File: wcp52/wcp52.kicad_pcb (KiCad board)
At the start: 4 copper layers, 100 x 100 mm, 337 parts, among them J1 MicroUSB-B, J2 IN1, J3 IN2, J4 OUT, J5 9V 300mA, J6 JLINK, J7 AUX, J8 AVR-ICSP, Q1 MMBT3906, Q10 MMBT3904, Q11 BFR540, Q12 BFR540, Q13 MMBT3904, Q14 MMBT3904, Q15 MMBT3904, Q16 MMBT3904, Q17 PZT2907A, Q18 PZT2907A, Q19 MMBT3904, Q2 IRLML6402, Q20 IRLML6402, Q3 AOD417, Q4 MMBT3906, Q5 2N7002, Q6 2N7002, Q7 MMBT3906, Q8 2N7002, Q9 2N7002, U1 TL431AIDBZ, U10 MASWSS0162, U11 AD8310ARMZ, U12 ATSAM4S16CA-AU, U13 FT230XS_DNP, U14 L78M05CDT, U15 MC79M05CDT, U16 AZ1117CH-1.8TRG1, U17 MCP1700T-vv02E/TT, U18 ATMEGA32U4-AU-DNP, U2 LM393M, U3 LMH6714MF, U4 AD9958BCPZ, U5 LMH6714MF, U6 AD8000YRDZ, U7 THS3001IDGN, U8 MAADSS0008, U9 MASWSS0162, X1 25 MHz, X2 12MHz

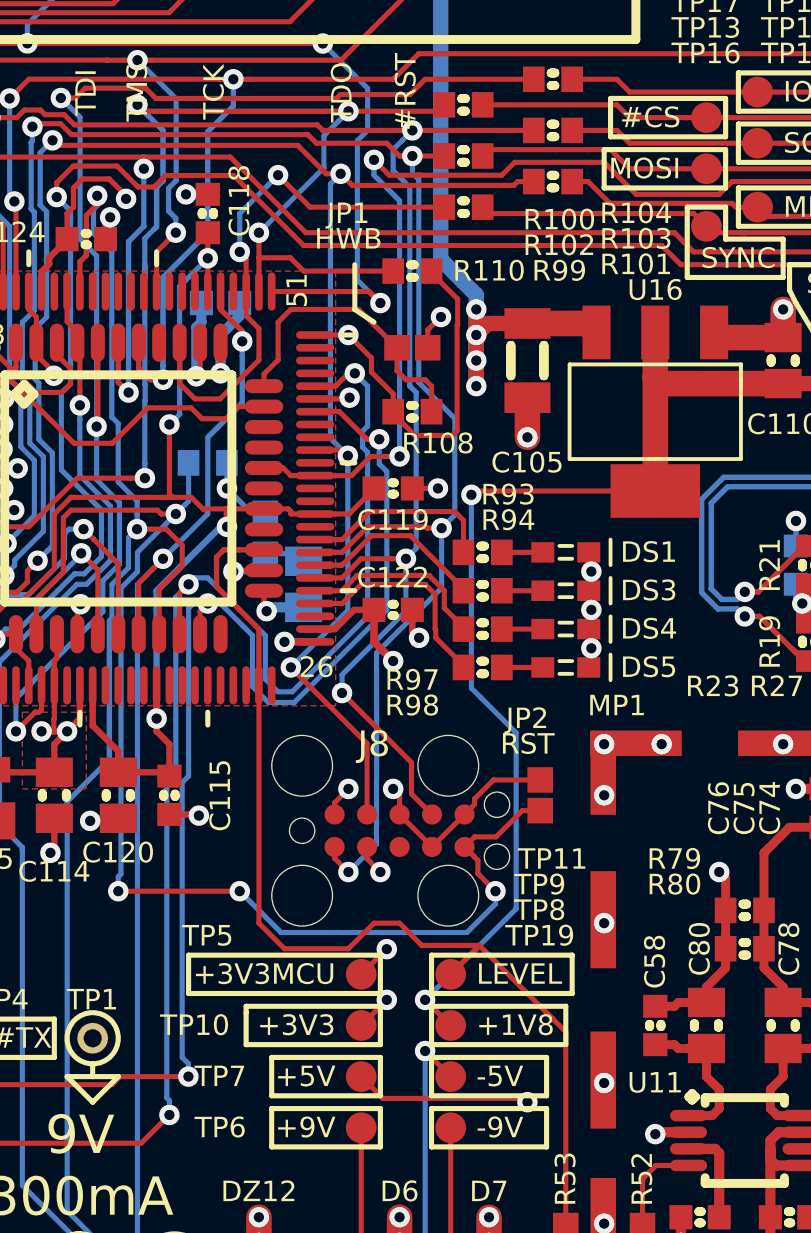
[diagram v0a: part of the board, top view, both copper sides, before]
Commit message: Route LEDs to AVR
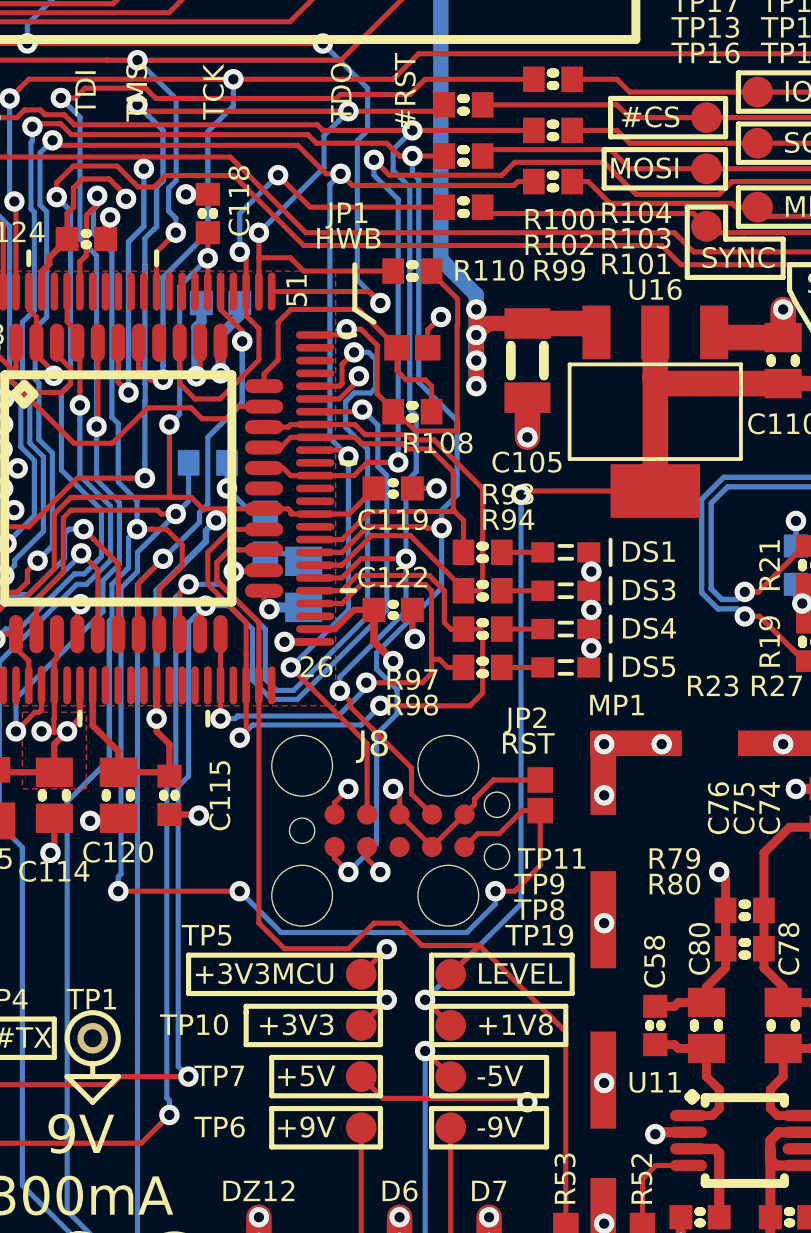
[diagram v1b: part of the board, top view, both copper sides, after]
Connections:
- J6 pad 1: Net-(J6-Pad1) -> +3.3SB
- J6 pad 17: (no net) -> Net-(J6-Pad17)
- U12 pad 21: Net-(U12-Pad21) -> /MPU/LED3
- U12 pad 23: Net-(U12-Pad23) -> /MPU/LED2
- U12 pad 42: Net-(U12-Pad42) -> /MPU/LED0
- U12 pad 43: Net-(U12-Pad43) -> /MPU/LED1
- U18 pad 22: Net-(U18-Pad22) -> /MPU/LED3
- U18 pad 26: Net-(U18-Pad26) -> /MPU/LED2
- U18 pad 30: Net-(U18-Pad30) -> /MPU/LED0
- U18 pad 31: Net-(U18-Pad31) -> /MPU/LED1
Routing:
- net /MPU/LED2: track 7.36 -> 31.6 mm, vias 0 -> 2
- net /MPU/LED1: track 7.21 -> 21.5 mm
- net /MPU/LED3: track 8.48 -> 22.1 mm, vias 0 -> 2
- net /MPU/LED0: track 7.65 -> 17.3 mm
- net /Comm/SER_FROMUSB: track 56.9 -> 59.9 mm
- net +1.8: track 64.4 -> 61.8 mm
- net /MPU/AVR#RST: track 49.6 -> 51.7 mm
- net /MPU/MOSI: track 73.8 -> 74.5 mm
- net GND: track 668.4 -> 669.0 mm

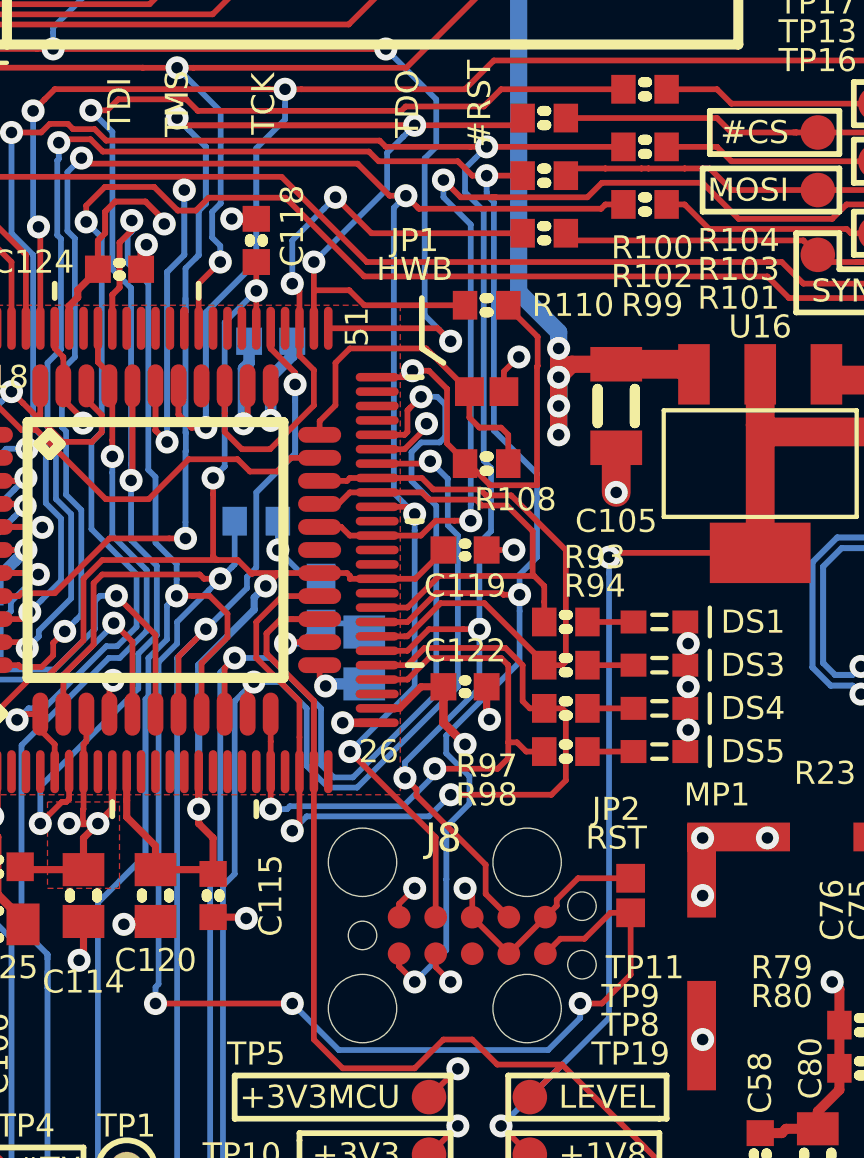
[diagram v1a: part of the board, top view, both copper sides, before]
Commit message: Remove extra connections
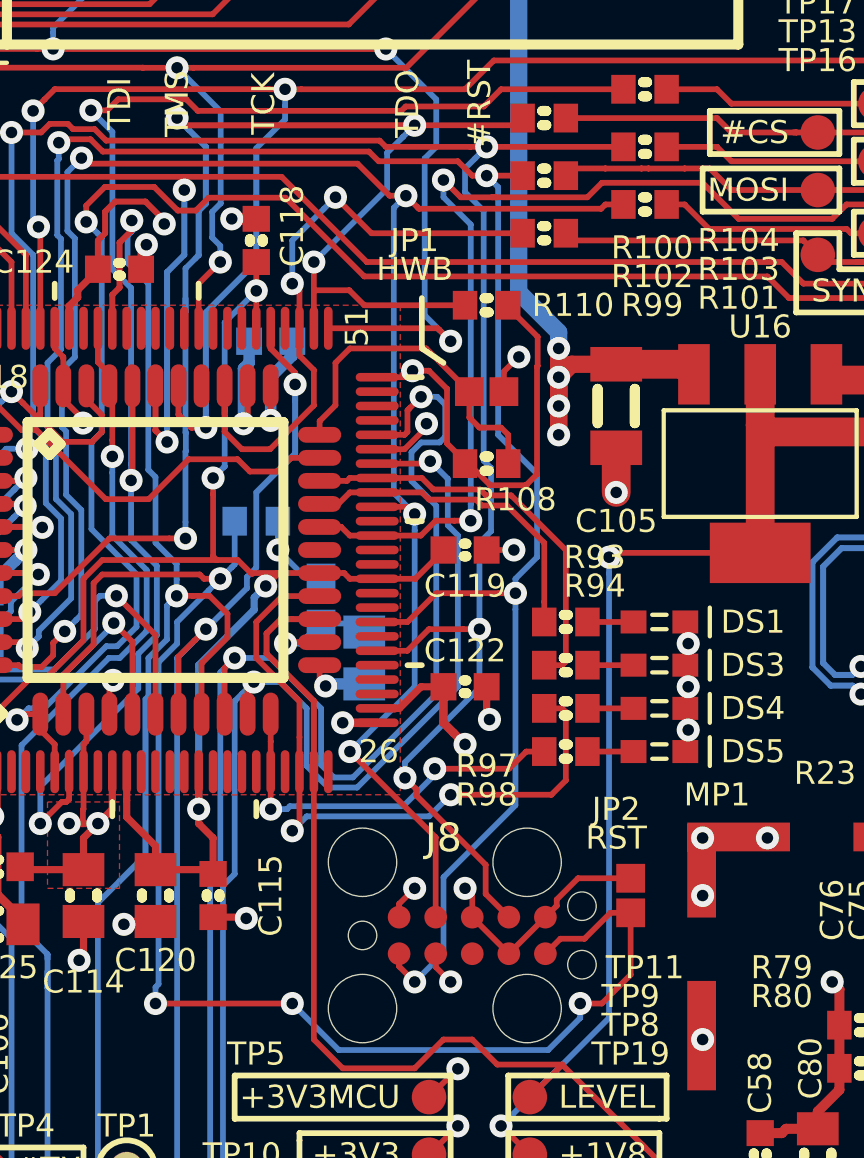
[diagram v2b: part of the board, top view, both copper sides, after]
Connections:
- U12 pad 29: /MPU/LED3 -> Net-(U12-Pad29)
- U12 pad 30: /MPU/LED2 -> Net-(U12-Pad30)
- U12 pad 32: /MPU/LED1 -> Net-(U12-Pad32)
- U12 pad 34: /MPU/LED0 -> Net-(U12-Pad34)
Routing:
- net /MPU/LED3: track 22.1 -> 13.8 mm
- net /MPU/LED2: track 31.6 -> 23.9 mm
- net /MPU/LED1: track 21.5 -> 14.4 mm
- net /MPU/LED0: track 17.3 -> 11.4 mm
- net /MPU/MOSI: track 74.5 -> 73.7 mm

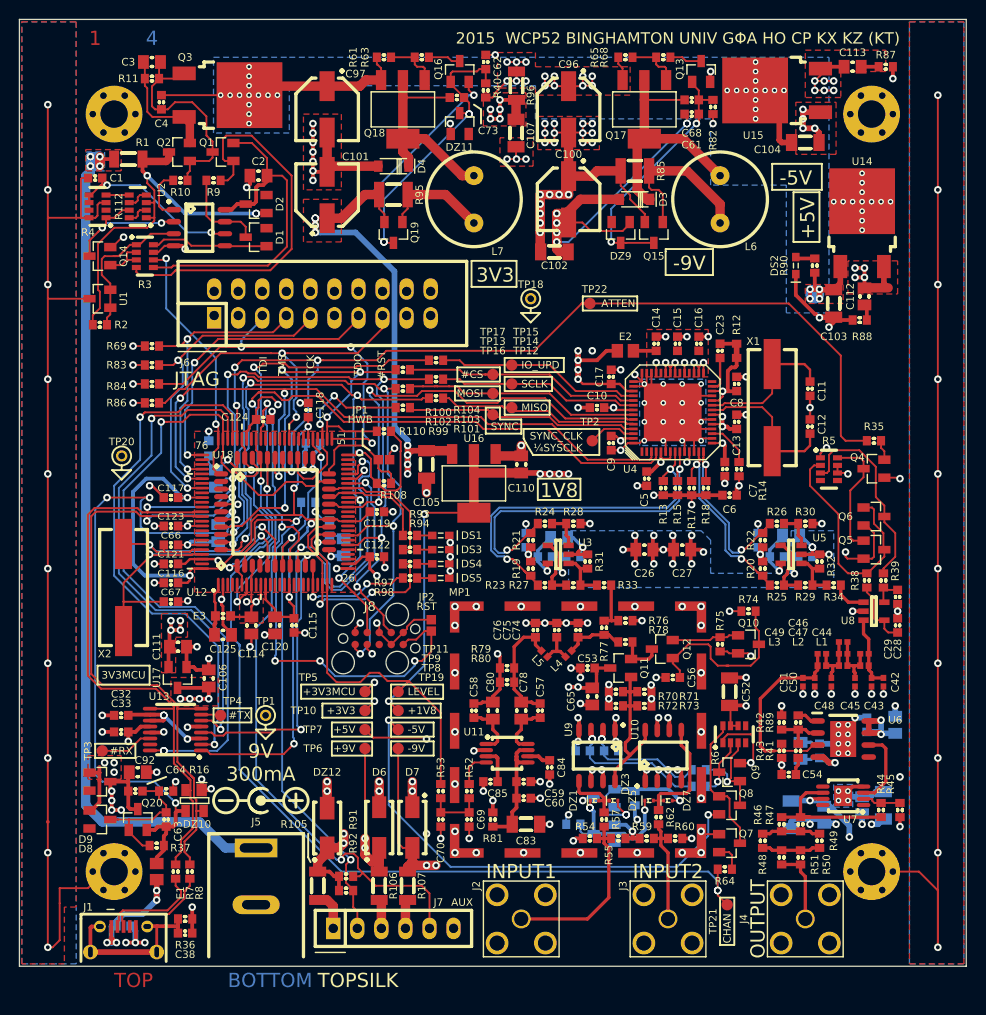
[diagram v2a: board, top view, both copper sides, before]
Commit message: Add PSU filter inductors
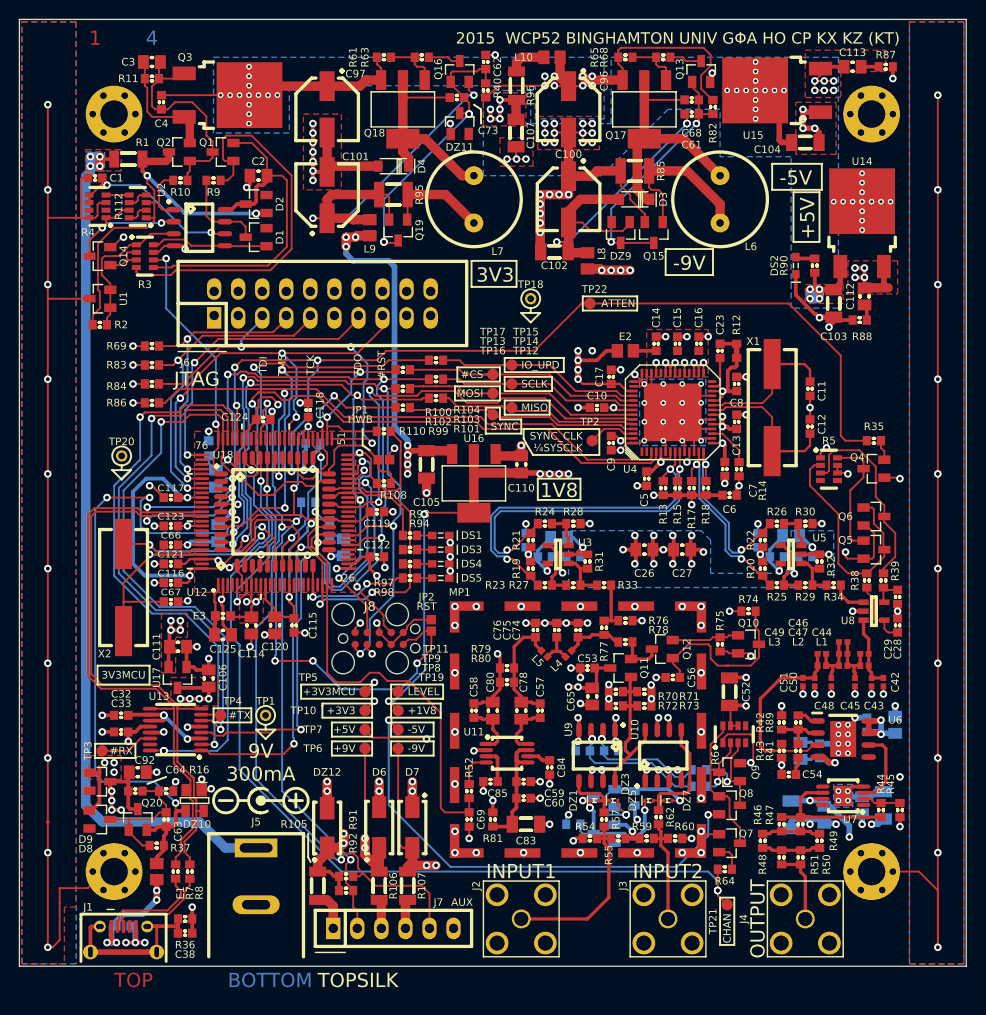
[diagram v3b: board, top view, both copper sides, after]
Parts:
- removed C70: 10n, IPC7351-Nominal:CAPC1608X55
- removed R53: 49R9, IPC7351-Nominal:RESC1608X50
- added L10: 4u7, IPC7351-Nominal:INDC2012X130, F.Cu at (131.2, 29.0)
- added L8: 4u7, IPC7351-Nominal:INDC2012X130, F.Cu at (135.0, 50.5)
- added L9: 4u7, IPC7351-Nominal:INDC2012X130, F.Cu at (112.0, 47.0)
- moved Q19 0.56 mm to (115.0, 47.2)
- turned R82 to 270 degrees
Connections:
- C100 pad 2: -9 -> Net-(C100-Pad2)
- C101 pad 1: +3.3 -> Net-(C101-Pad1)
- C102 pad 2: -9 -> Net-(C100-Pad2)
- C103 pad 1: /DCDC/IN -> +9
- C61 pad 2: -9 -> Net-(C100-Pad2)
- C69 pad 1: Net-(C69-Pad1) -> /MPU/ADIN
- D3 pad 2: -9 -> Net-(C100-Pad2)
- DZ9 pad 1: -9 -> Net-(C100-Pad2)
- Q16 pad 2: +3.3 -> Net-(C101-Pad1)
- Q19 pad 2: +3.3 -> Net-(C101-Pad1)
- R52 pad 1: Net-(C69-Pad1) -> /MPU/ADIN
- R90 pad 1: /DCDC/IN -> +9
- R95 pad 1: +3.3 -> Net-(C101-Pad1)
- R96 pad 1: /DCDC/IN -> Net-(L10-Pad1)
- U14 pad 1: /DCDC/IN -> +9
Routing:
- net -9: track 303.5 -> 248.7 mm, vias 26 -> 24
- net Net-(C101-Pad1): track 0.00 -> 41.4 mm, vias 0 -> 2
- net Net-(C100-Pad2): track 0.00 -> 41.1 mm, vias 0 -> 3
- net +3.3: track 93.2 -> 58.1 mm, vias 13 -> 11
- net +9: track 234.7 -> 245.2 mm, vias 9 -> 13
- net /DCDC/IN: track 82.2 -> 91.8 mm, vias 32 -> 21
- net /MPU/ADIN: track 40.7 -> 47.9 mm
- net Net-(C69-Pad1): track 6.00 -> 0.00 mm
- net Net-(L10-Pad1): track 0.00 -> 4.11 mm
- net +5: track 232.8 -> 234.2 mm
- net GND: track 669.0 -> 667.6 mm, vias 255 -> 254
- net /MPU/AVR#RST: track 51.7 -> 53.0 mm
- net /DCDC/FDBK_3V3: track 29.8 -> 30.4 mm
- net (no net): track 0.07 -> 0.00 mm, vias 2 -> 1
- added copper zone on B.Cu, net +9
- removed copper zone on F.Cu, net +3.3

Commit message: Test point fixes
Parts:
- TP3: value #RX -> RX
- TP4: value #TX -> TX
- moved TP3 15.4 mm to (99.0, 100.5)
- moved TP1 3.50 mm to (101.0, 95.0)
- moved TP4 2.75 mm to (99.0, 98.5)
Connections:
- TP3 pad 1: Net-(TP3-Pad1) -> /Comm/SER_FROMUSB
- TP4 pad 1: Net-(TP4-Pad1) -> /MPU/SER_FROM_MPU
- U13 pad 14: Net-(TP3-Pad1) -> Net-(U13-Pad14)
- U13 pad 7: Net-(TP4-Pad1) -> Net-(U13-Pad7)
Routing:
- net Net-(TP3-Pad1): track 5.59 -> 0.00 mm
- net Net-(TP4-Pad1): track 2.08 -> 0.00 mm
- net /Comm/#CTS: track 54.6 -> 53.2 mm
- net /MPU/SER_FROM_MPU: track 52.5 -> 51.4 mm
- net /Comm/SER_FROMUSB: track 59.9 -> 59.3 mm
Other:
- board text added: "RX"
- board text added: "TX"
- board text removed: "#RX"
- board text removed: "#TX"

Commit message: Add back drawing
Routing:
- net GND: track 667.6 -> 668.4 mm
- net Net-(D2-Pad1): track 42.6 -> 43.2 mm
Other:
- board text added: "+5V LINEAR REGULATOR"
- board text added: "-5V LINEAR REGULATOR"
- board text added: "-9V DC-DC CONVERTER"
- board text added: "3.3V DC-DC CONVERTER"
- board text added: "AMP"
- board text added: "ATTEN CONTROL"
- board text added: "BUFFER"
- board text added: "BUFFER BIASING"
- board text added: "CHAN SEL"
- board text added: "CHAN SEL SWITCH BIASING"
- board text added: "FILTER"
- board text added: "LOGARITHMIC DETECTOR"
- board text added: "MICROCONTROLLER"
- board text added: "OUTPUT SIGNAL"
- board text added: "PHASE REFERENCE SIGNAL"
- board text added: "POWER"
- board text added: "REVERSE POLARITY PROTECTION, RESETTABLE FUSE, UNDERVOLT LOCKOUT, OVERVOLT LOCKOUT, INRUSH LIMITING"
- board text added: "SINE WAVE SYNTHESIZER"
- board text added: "SPI"
- board text added: "SWITCHED ATTENUATOR"
- board text added: "TERMINATION"
- board text added: "USB"
- board text added: "Σ"

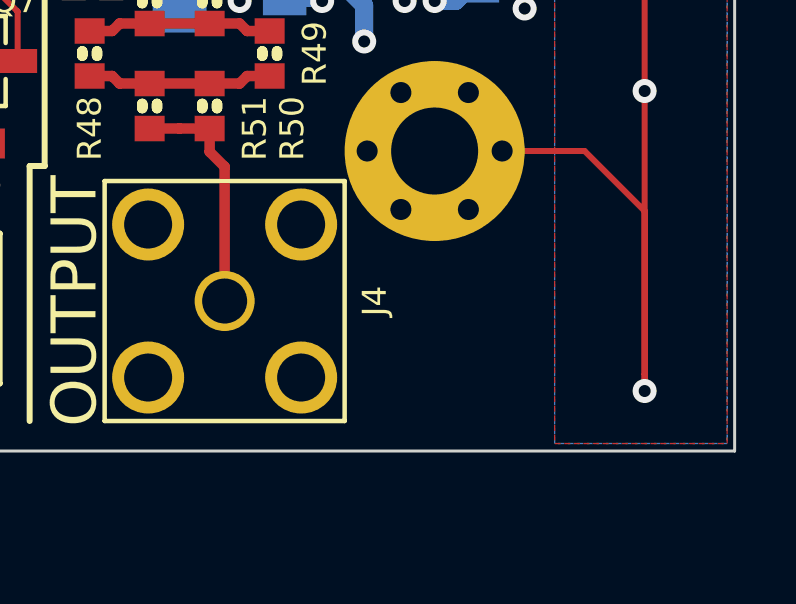
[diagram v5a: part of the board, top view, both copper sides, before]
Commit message: Add panel power LED
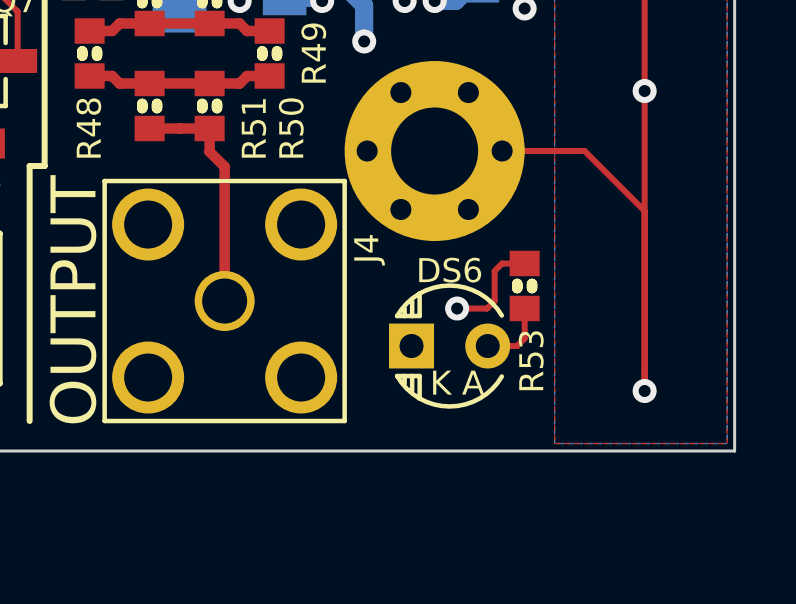
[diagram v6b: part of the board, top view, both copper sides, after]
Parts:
- added DS6: PWR, pth-semi:LED-3mm, F.Cu at (165.5, 121.5)
- added R53: 3k3, IPC7351-Nominal:RESC1608X50, F.Cu at (168.0, 119.5)
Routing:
- net +9: track 245.2 -> 259.8 mm, vias 13 -> 14
- net Net-(DS6-Pad2): track 0.00 -> 2.33 mm
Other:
- board text added: "K A"
